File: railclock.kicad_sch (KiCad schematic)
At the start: 175 parts, among them J1 Conn_01x02_Pin, J10 Conn_01x04_MountingPin, J11 Conn_01x04_MountingPin, J12 Conn_01x04_MountingPin, J13 Conn_01x04_MountingPin, J14 Conn_01x04_MountingPin, J15 Conn_01x03_MountingPin, J16 Barrel_Jack_Switch, J2 Conn_01x03_MountingPin, J3 Conn_01x04_MountingPin, J4 USB_C_Receptacle_USB2.0_14P, J5 Conn_01x03_MountingPin, J6 Conn_01x03_MountingPin, J7 Conn_01x03_MountingPin, J8 Conn_01x03_MountingPin, J9 Conn_01x04_MountingPin, Q1 Q_NPN_BEC, SW1 SW_SPST, SW2 SW_DPDT_x2, U1 MCP7940N-xST, U10 74AHC1G04, U11 MAX811TEUS-T, U12 MCP4728, U13 BTS5012SDA, U14 BTS5012SDA, U15 BTS5012SDA, U16 BTS5012SDA, U17 BTS5012SDA, U2 MCP73832-2-OT, U4 ESP32-C6-WROOM-1, U5 DRV8870DDA, U6 PAM2421, U8 BQ24296MRGET, U9 PCF8574RGTR, Y2 Crystal_GND3

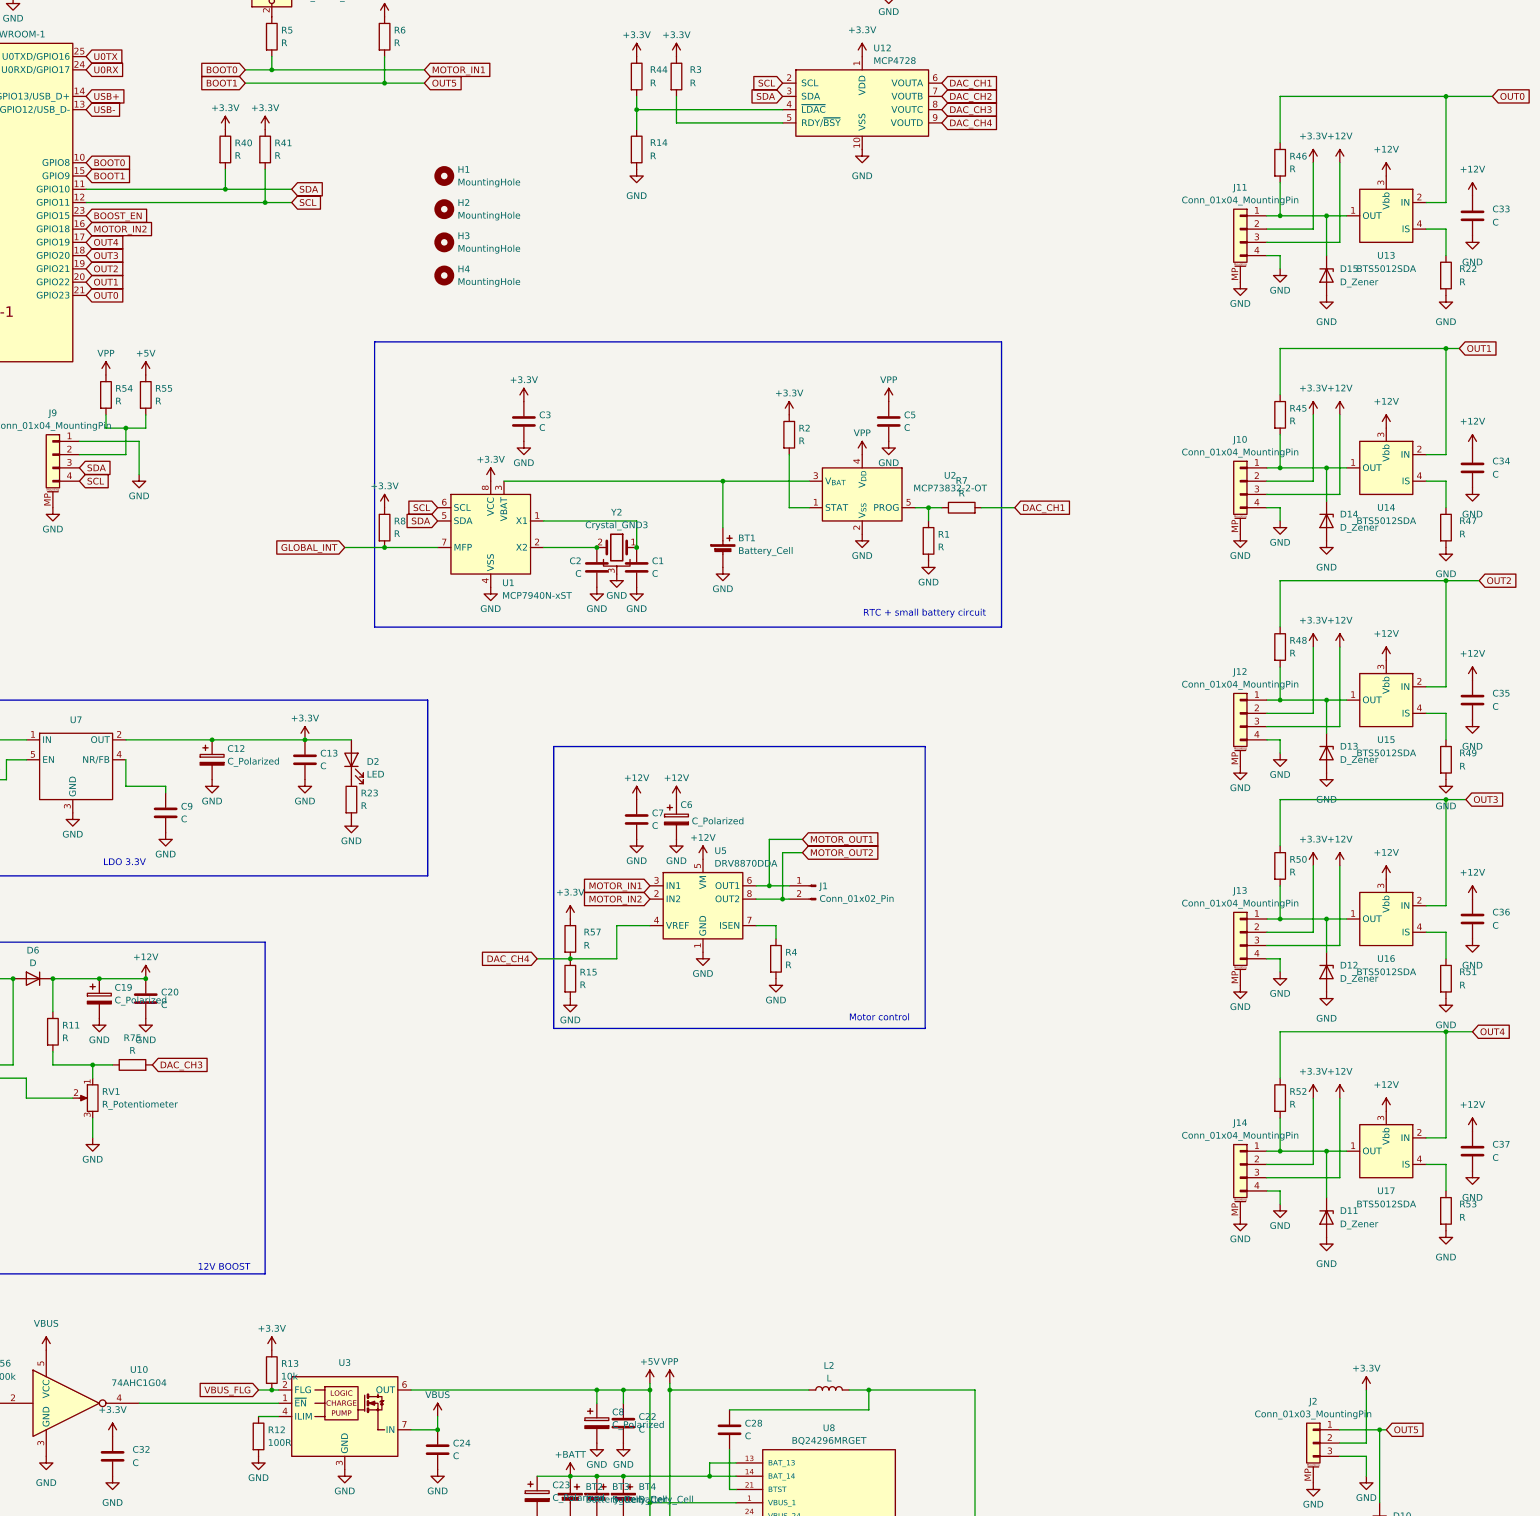
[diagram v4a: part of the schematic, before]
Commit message: Add transils fix vbus detection
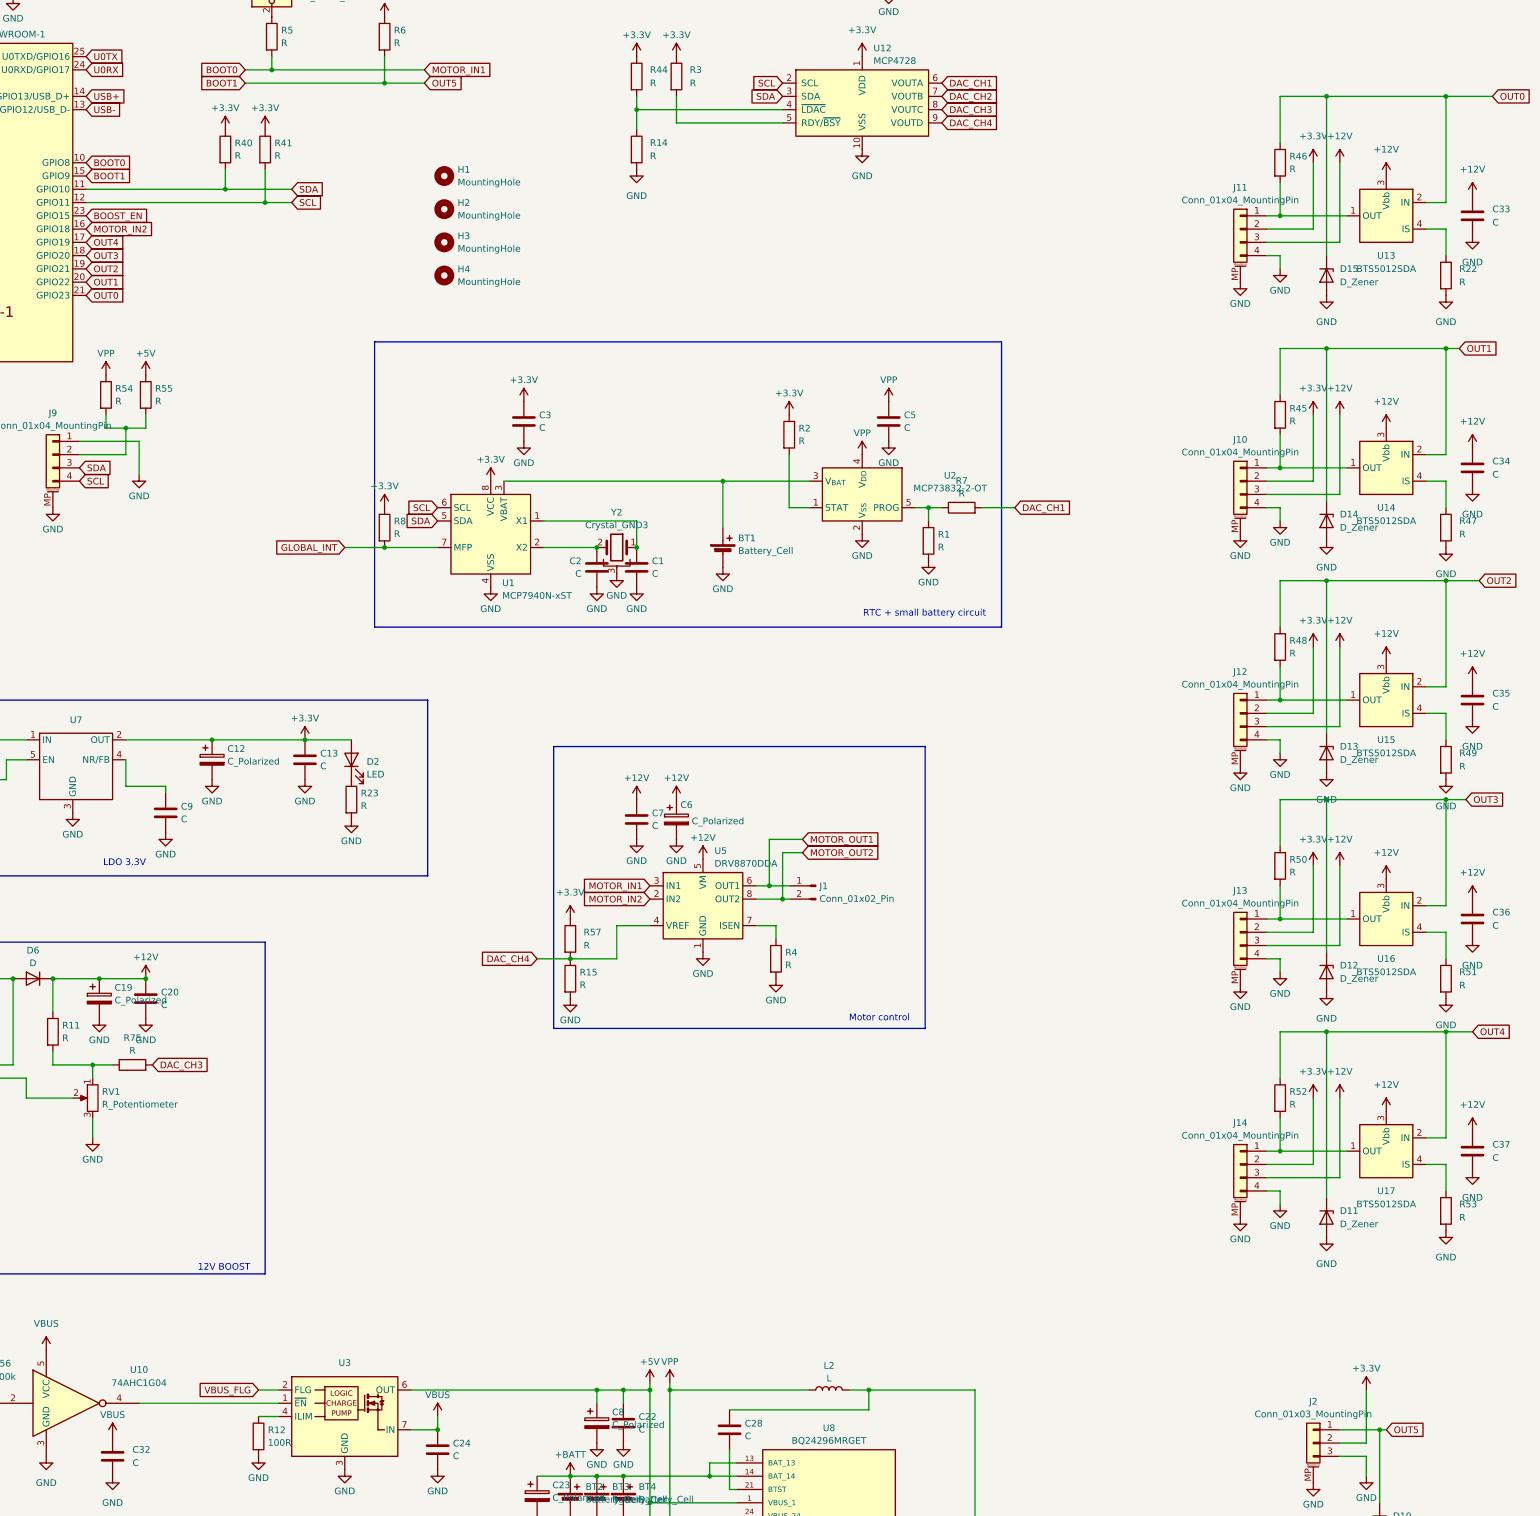
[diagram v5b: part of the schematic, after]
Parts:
- removed R13: 10k, Resistor_SMD:R_0805_2012Metric, symbol Device:R
- D10, D11, D12, D13, D14, D15, D3, D4, D5, D7, D8, D9: footprint (none) -> Diode_SMD:D_SOD-323
- Q1: footprint (none) -> Package_TO_SOT_SMD:SOT-23
- R21, R56, R57: footprint (none) -> Resistor_SMD:R_0805_2012Metric
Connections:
- net +3.3V: no longer C32.1
- net IN: now also C32.1
- net OUT0: now also D15.1 (K)
- net OUT1: now also D14.1 (K)
- net OUT2: now also D13.1 (K)
- net OUT3: now also D12.1 (K)
- net OUT4: now also D11.1 (K)
- net at J12.1 (Pin_1), R48.2, U15.1 (OUT)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: no longer D13.1 (K)
- net at J13.1 (Pin_1), R50.2, U16.1 (OUT)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: no longer D12.1 (K)
- net at J14.1 (Pin_1), R52.2, U17.1 (OUT)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: no longer D11.1 (K)
- net at J10.1 (Pin_1), R45.2, U14.1 (OUT)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: no longer D14.1 (K)
- net at J11.1 (Pin_1), R46.2, U13.1 (OUT)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: no longer D15.1 (K)

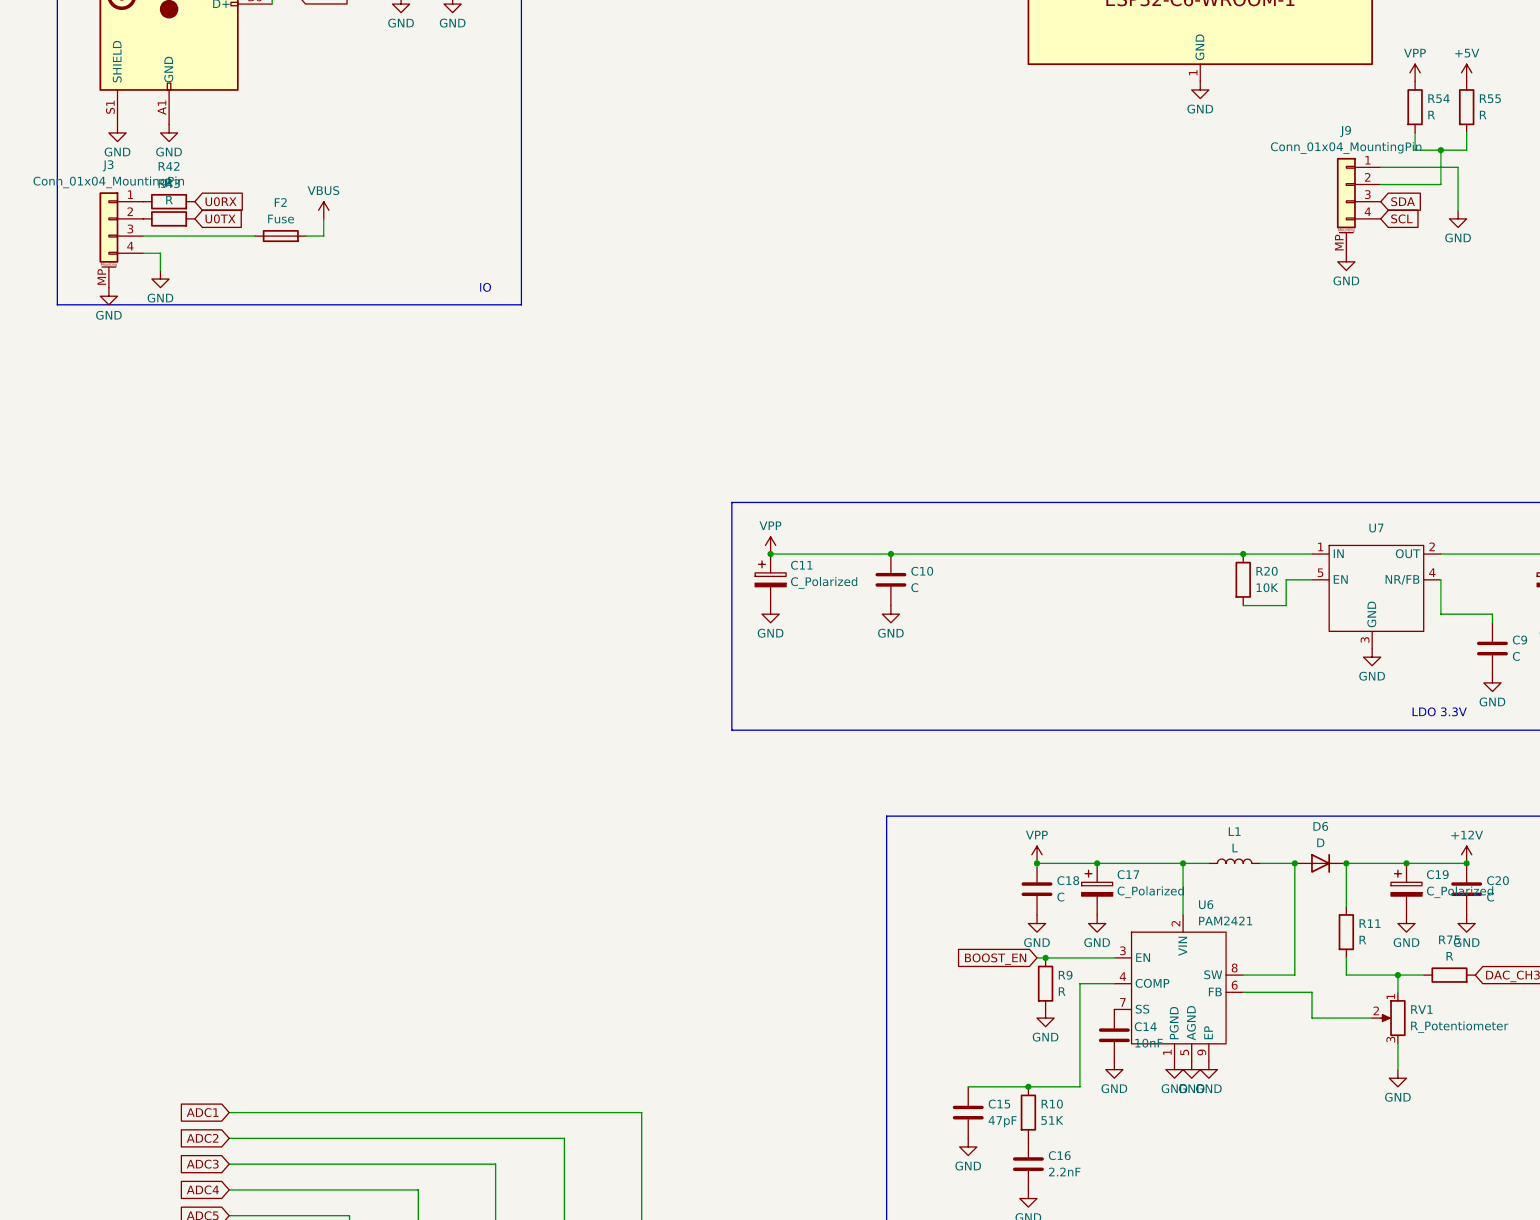
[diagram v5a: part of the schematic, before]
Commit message: Replace UART connector
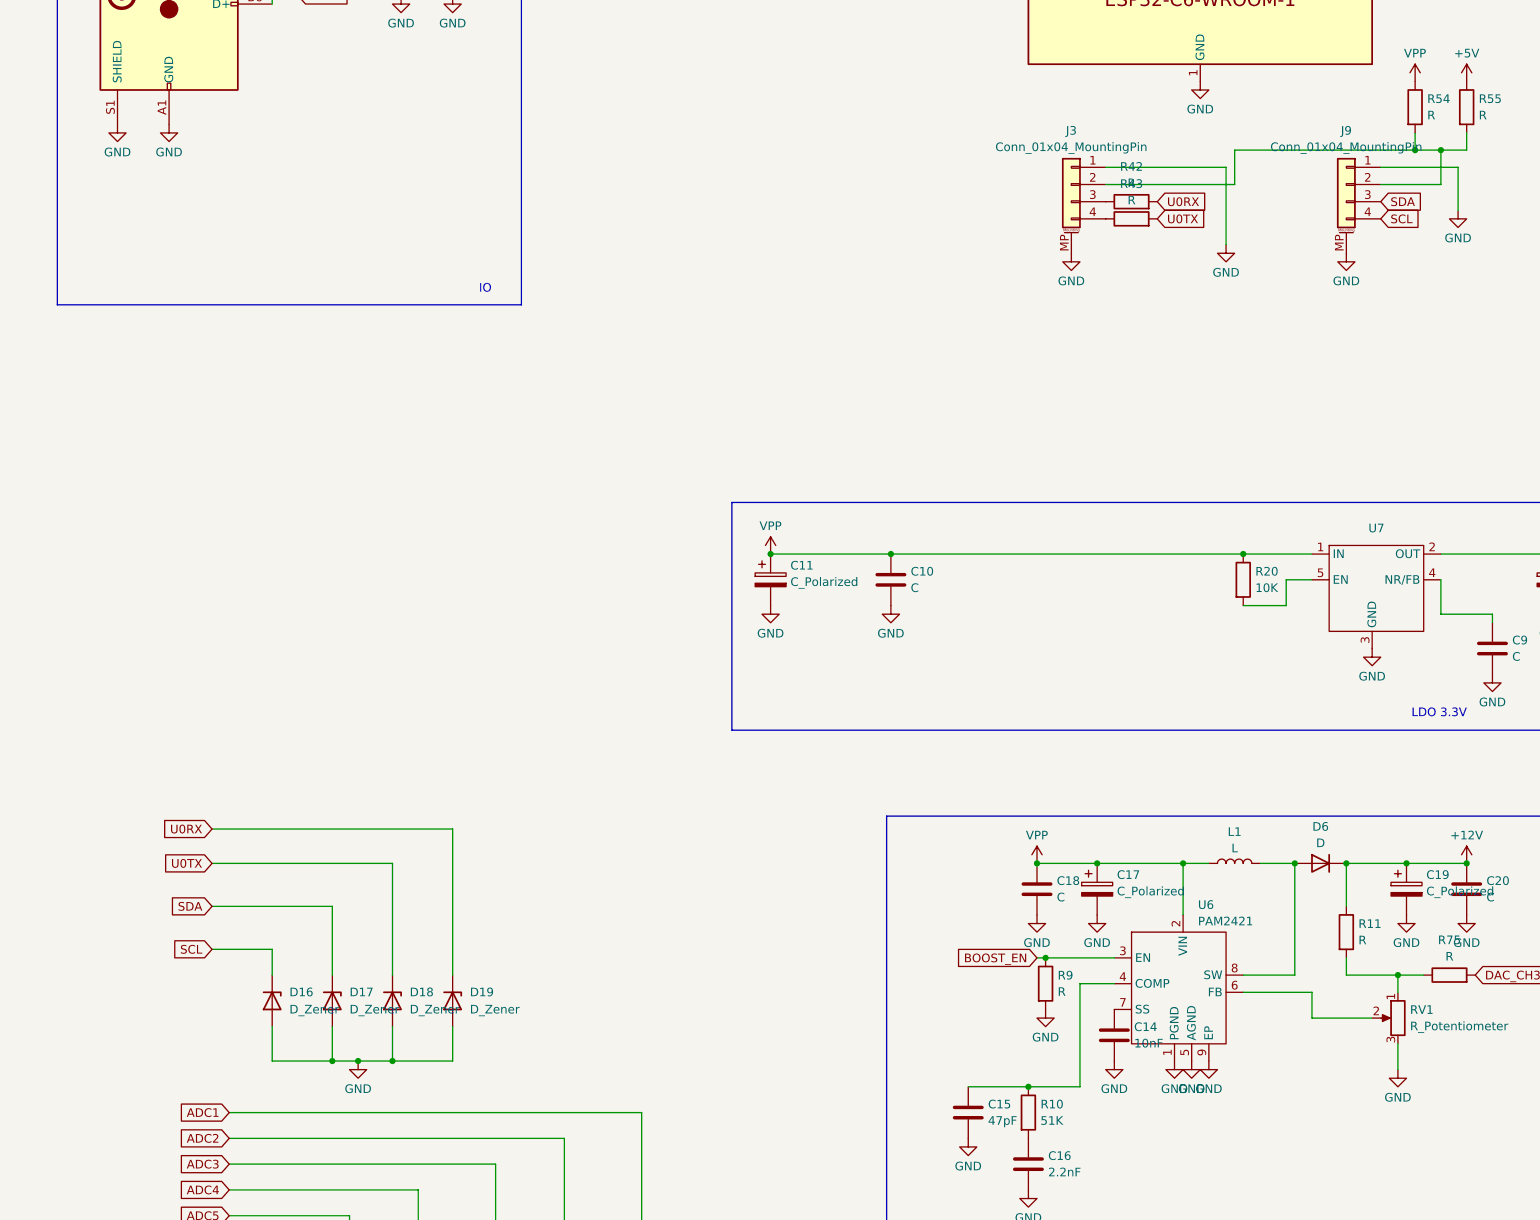
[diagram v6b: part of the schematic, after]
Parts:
- removed F2: Fuse, Fuse:Fuse_1206_3216Metric, symbol Device:Fuse
- added D16, D17, D18, D19: D_Zener, Diode_SMD:D_SOD-323, symbol Device:D_Zener
- J3: footprint Connector_JST:JST_SH_SM04B-SRSS-TB_1x04-1MP_P1.00mm_Horizontal -> Connector_JST:JST_PH_S4B-PH-SM4-TB_1x04-1MP_P2.00mm_Horizontal
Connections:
- net GND: now also J3.1 (Pin_1), D16.2 (A), D17.2 (A), D18.2 (A), D19.2 (A); no longer J3.4 (Pin_4)
- net SCL: now also D16.1 (K)
- net SDA: now also D17.1 (K)
- net U0RX: now also D19.1 (K)
- net U0TX: now also D18.1 (K)
- net at J9.2 (Pin_2), R54.2, R55.2: now also J3.2 (Pin_2)
- net at J3.3 (Pin_3): now also R42.1
- net at R43.1: now also J3.4 (Pin_4); no longer J3.2 (Pin_2)
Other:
- moved on the sheet: J3, R42, R43
